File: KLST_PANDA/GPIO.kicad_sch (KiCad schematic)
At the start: 0 parts

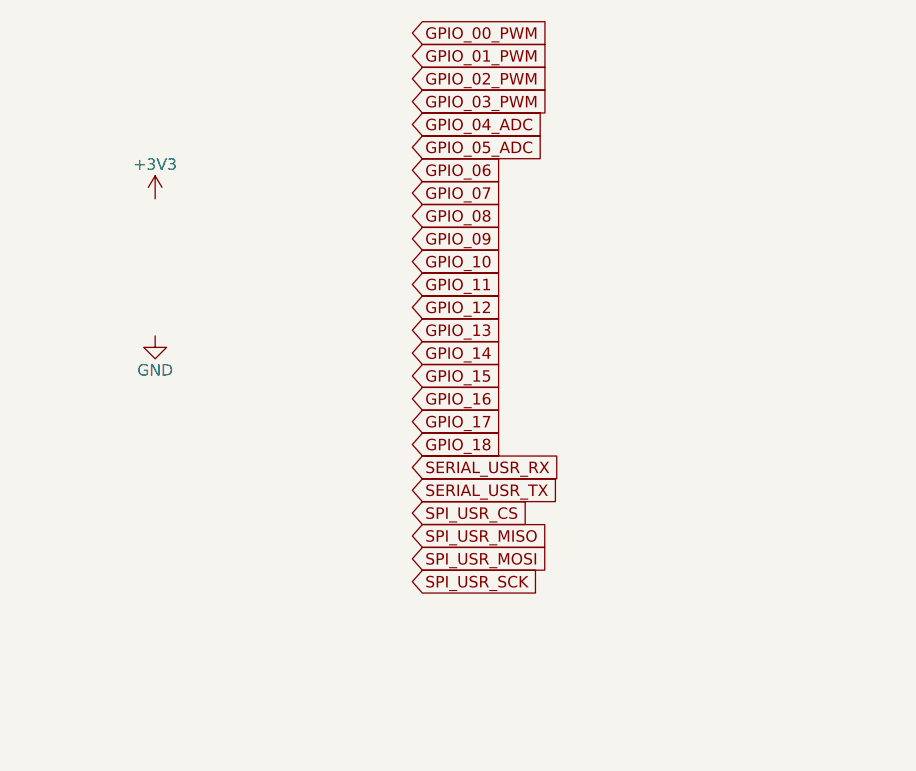
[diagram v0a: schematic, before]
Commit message: improved GPIO, updated schematics
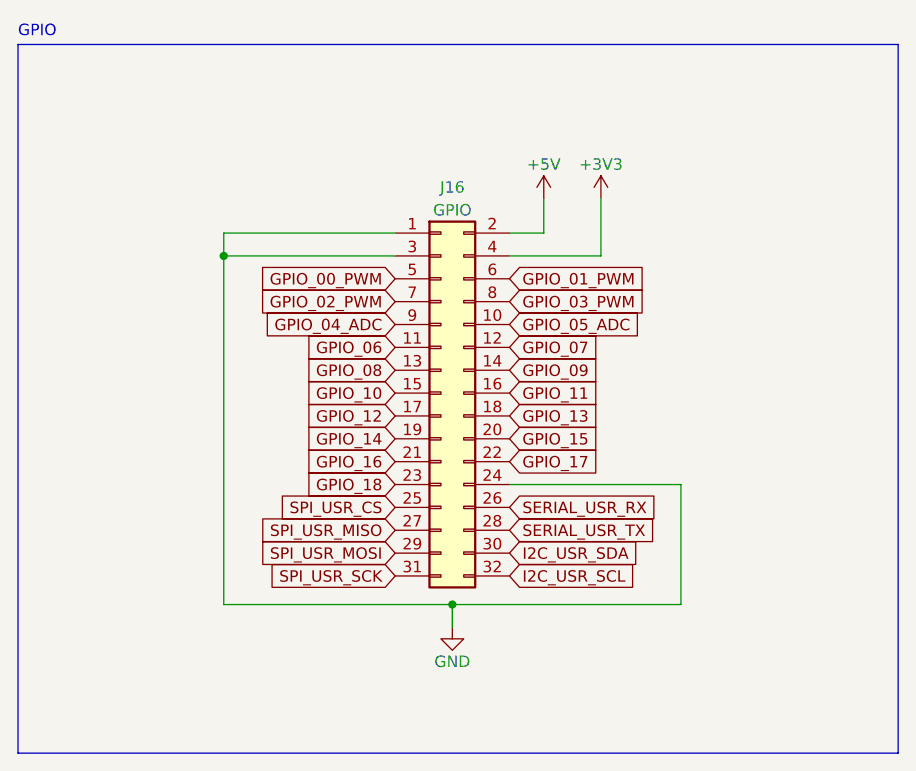
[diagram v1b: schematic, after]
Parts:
- added J16: GPIO, symbol Connector_Generic:Conn_02x16_Odd_Even
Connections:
- net +3V3: now also J16.4 (Pin_4)
- net GND: now also J16.1 (Pin_1), J16.24 (Pin_24), J16.3 (Pin_3)
- net GPIO_00_PWM: now also J16.5 (Pin_5)
- net GPIO_01_PWM: now also J16.6 (Pin_6)
- net GPIO_02_PWM: now also J16.7 (Pin_7)
- net GPIO_03_PWM: now also J16.8 (Pin_8)
- net GPIO_04_ADC: now also J16.9 (Pin_9)
- net GPIO_05_ADC: now also J16.10 (Pin_10)
- net GPIO_06: now also J16.11 (Pin_11)
- net GPIO_07: now also J16.12 (Pin_12)
- net GPIO_08: now also J16.13 (Pin_13)
- net GPIO_09: now also J16.14 (Pin_14)
- net GPIO_10: now also J16.15 (Pin_15)
- net GPIO_11: now also J16.16 (Pin_16)
- net GPIO_12: now also J16.17 (Pin_17)
- net GPIO_13: now also J16.18 (Pin_18)
- net GPIO_14: now also J16.19 (Pin_19)
- net GPIO_15: now also J16.20 (Pin_20)
- net GPIO_16: now also J16.21 (Pin_21)
- net GPIO_17: now also J16.22 (Pin_22)
- net GPIO_18: now also J16.23 (Pin_23)
- net SERIAL_USR_RX: now also J16.26 (Pin_26)
- net SERIAL_USR_TX: now also J16.28 (Pin_28)
- net SPI_USR_CS: now also J16.25 (Pin_25)
- net SPI_USR_MISO: now also J16.27 (Pin_27)
- net SPI_USR_MOSI: now also J16.29 (Pin_29)
- net SPI_USR_SCK: now also J16.31 (Pin_31)
- new net +5V: J16.2 (Pin_2)
- new net I2C_USR_SCL: J16.32 (Pin_32)
- new net I2C_USR_SDA: J16.30 (Pin_30)
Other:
- note added: "GPIO"

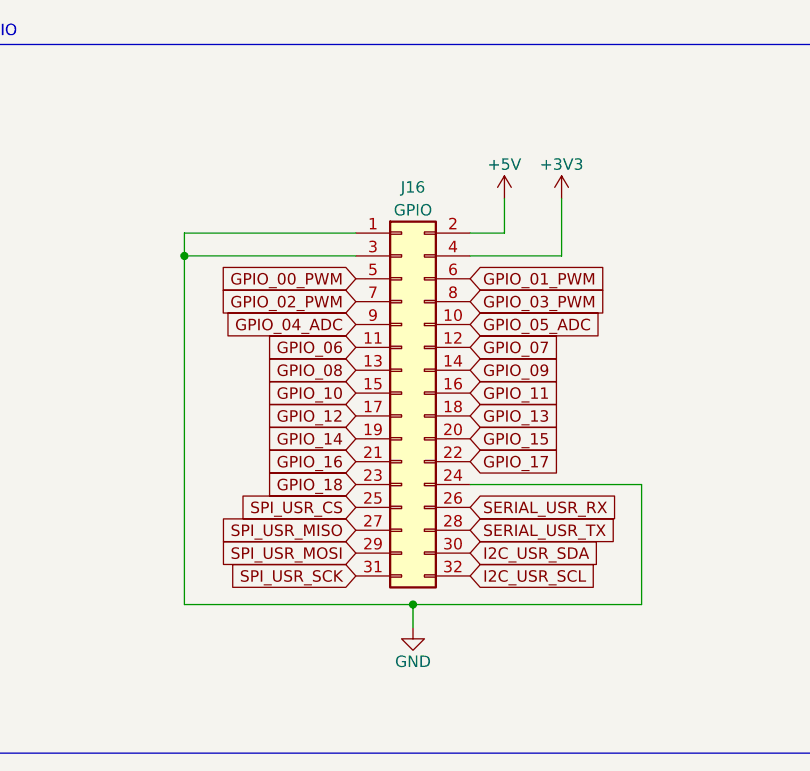
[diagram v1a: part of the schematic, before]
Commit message: added PDM interface ( and removed SAI )
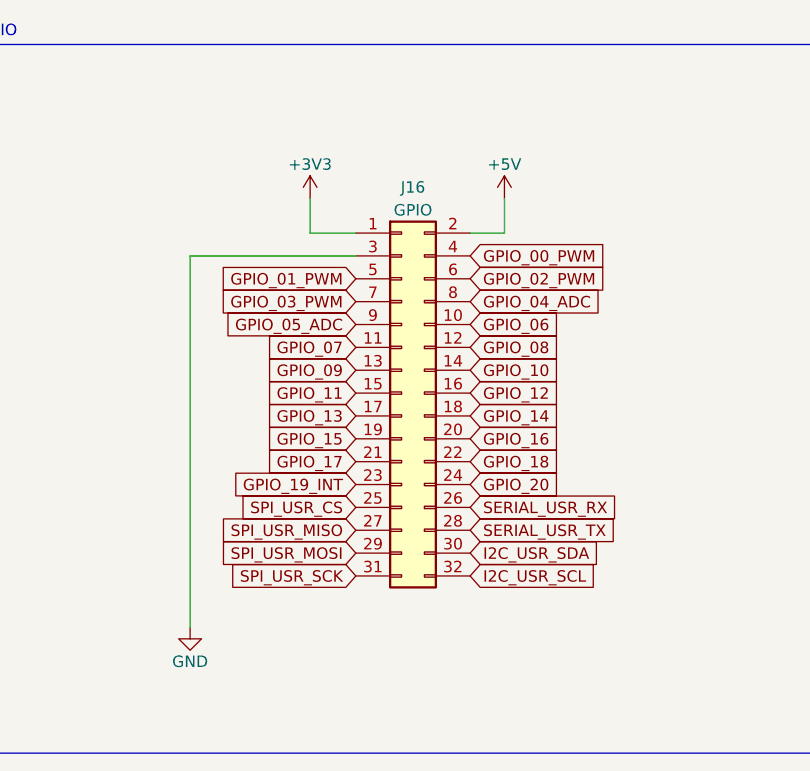
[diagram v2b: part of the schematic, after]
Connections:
- net +3V3: now also J16.1 (Pin_1); no longer J16.4 (Pin_4)
- net GND: no longer J16.1 (Pin_1), J16.24 (Pin_24)
- net GPIO_00_PWM: now also J16.4 (Pin_4); no longer J16.5 (Pin_5)
- net GPIO_01_PWM: now also J16.5 (Pin_5); no longer J16.6 (Pin_6)
- net GPIO_02_PWM: now also J16.6 (Pin_6); no longer J16.7 (Pin_7)
- net GPIO_03_PWM: now also J16.7 (Pin_7); no longer J16.8 (Pin_8)
- net GPIO_04_ADC: now also J16.8 (Pin_8); no longer J16.9 (Pin_9)
- net GPIO_05_ADC: now also J16.9 (Pin_9); no longer J16.10 (Pin_10)
- net GPIO_06: now also J16.10 (Pin_10); no longer J16.11 (Pin_11)
- net GPIO_07: now also J16.11 (Pin_11); no longer J16.12 (Pin_12)
- net GPIO_08: now also J16.12 (Pin_12); no longer J16.13 (Pin_13)
- net GPIO_09: now also J16.13 (Pin_13); no longer J16.14 (Pin_14)
- net GPIO_10: now also J16.14 (Pin_14); no longer J16.15 (Pin_15)
- net GPIO_11: now also J16.15 (Pin_15); no longer J16.16 (Pin_16)
- net GPIO_12: now also J16.16 (Pin_16); no longer J16.17 (Pin_17)
- net GPIO_13: now also J16.17 (Pin_17); no longer J16.18 (Pin_18)
- net GPIO_14: now also J16.18 (Pin_18); no longer J16.19 (Pin_19)
- net GPIO_15: now also J16.19 (Pin_19); no longer J16.20 (Pin_20)
- net GPIO_16: now also J16.20 (Pin_20); no longer J16.21 (Pin_21)
- net GPIO_17: now also J16.21 (Pin_21); no longer J16.22 (Pin_22)
- net GPIO_18: now also J16.22 (Pin_22); no longer J16.23 (Pin_23)
- new net GPIO_19_INT: J16.23 (Pin_23)
- new net GPIO_20: J16.24 (Pin_24)

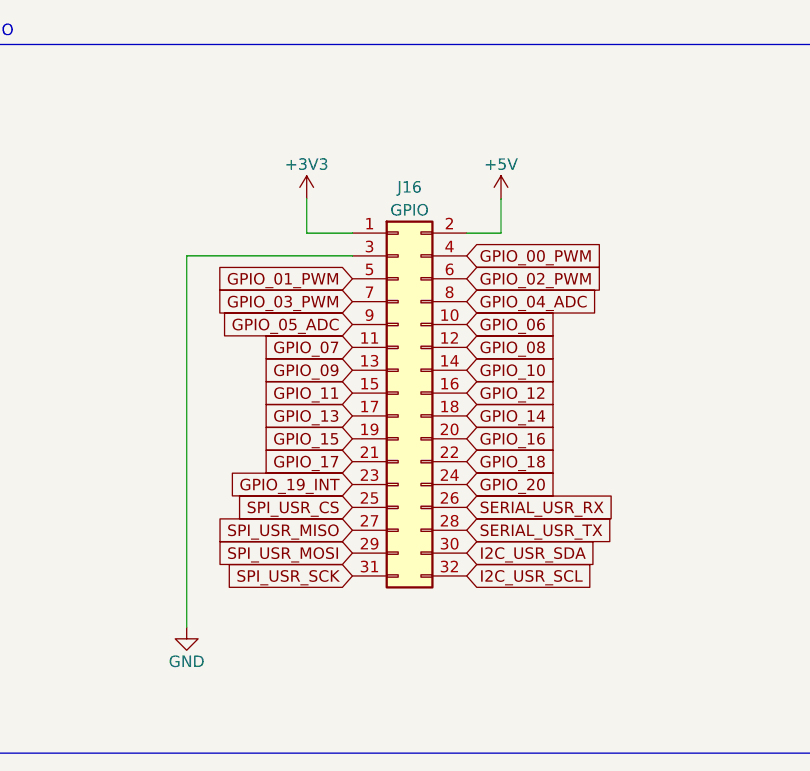
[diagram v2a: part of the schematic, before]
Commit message: added mechanical keys, updated audio jacks, minor changes
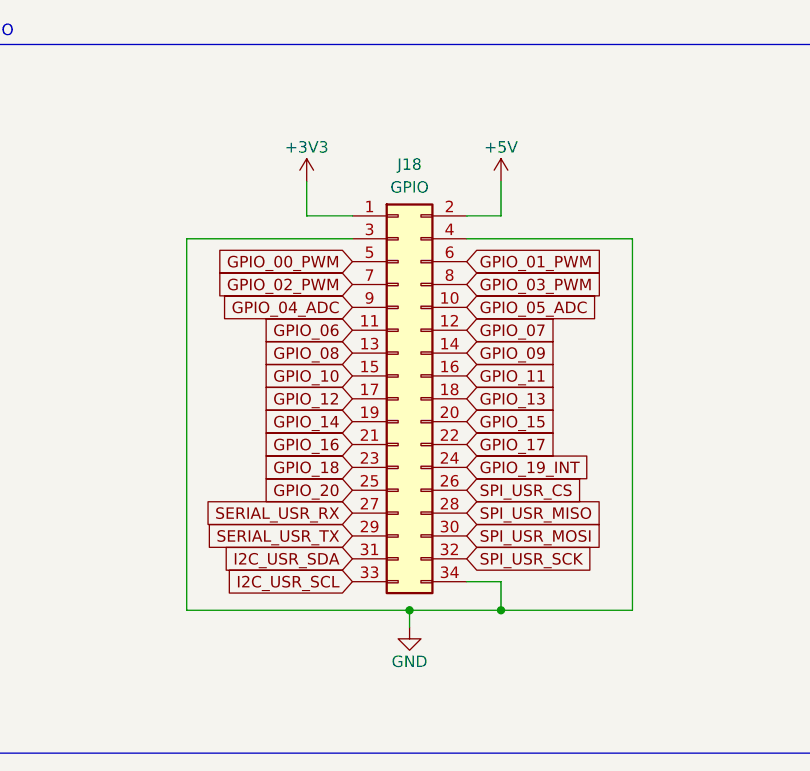
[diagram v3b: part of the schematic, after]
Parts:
- removed J16: GPIO, symbol Connector_Generic:Conn_02x16_Odd_Even
- added J18: GPIO, Connector_IDC:IDC-Header_2x17_P2.54mm_Horizontal, symbol Connector_Generic:Conn_02x17_Odd_Even
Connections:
- net +3V3: now also J18.1 (Pin_1)
- net +5V: now also J18.2 (Pin_2)
- net GND: now also J18.3 (Pin_3), J18.34 (Pin_34), J18.4 (Pin_4)
- net GPIO_00_PWM: now also J18.5 (Pin_5)
- net GPIO_01_PWM: now also J18.6 (Pin_6)
- net GPIO_02_PWM: now also J18.7 (Pin_7)
- net GPIO_03_PWM: now also J18.8 (Pin_8)
- net GPIO_04_ADC: now also J18.9 (Pin_9)
- net GPIO_05_ADC: now also J18.10 (Pin_10)
- net GPIO_06: now also J18.11 (Pin_11)
- net GPIO_07: now also J18.12 (Pin_12)
- net GPIO_08: now also J18.13 (Pin_13)
- net GPIO_09: now also J18.14 (Pin_14)
- net GPIO_10: now also J18.15 (Pin_15)
- net GPIO_11: now also J18.16 (Pin_16)
- net GPIO_12: now also J18.17 (Pin_17)
- net GPIO_13: now also J18.18 (Pin_18)
- net GPIO_14: now also J18.19 (Pin_19)
- net GPIO_15: now also J18.20 (Pin_20)
- net GPIO_16: now also J18.21 (Pin_21)
- net GPIO_17: now also J18.22 (Pin_22)
- net GPIO_18: now also J18.23 (Pin_23)
- net GPIO_19_INT: now also J18.24 (Pin_24)
- net GPIO_20: now also J18.25 (Pin_25)
- net I2C_USR_SCL: now also J18.33 (Pin_33)
- net I2C_USR_SDA: now also J18.31 (Pin_31)
- net SERIAL_USR_RX: now also J18.27 (Pin_27)
- net SERIAL_USR_TX: now also J18.29 (Pin_29)
- net SPI_USR_CS: now also J18.26 (Pin_26)
- net SPI_USR_MISO: now also J18.28 (Pin_28)
- net SPI_USR_MOSI: now also J18.30 (Pin_30)
- net SPI_USR_SCK: now also J18.32 (Pin_32)

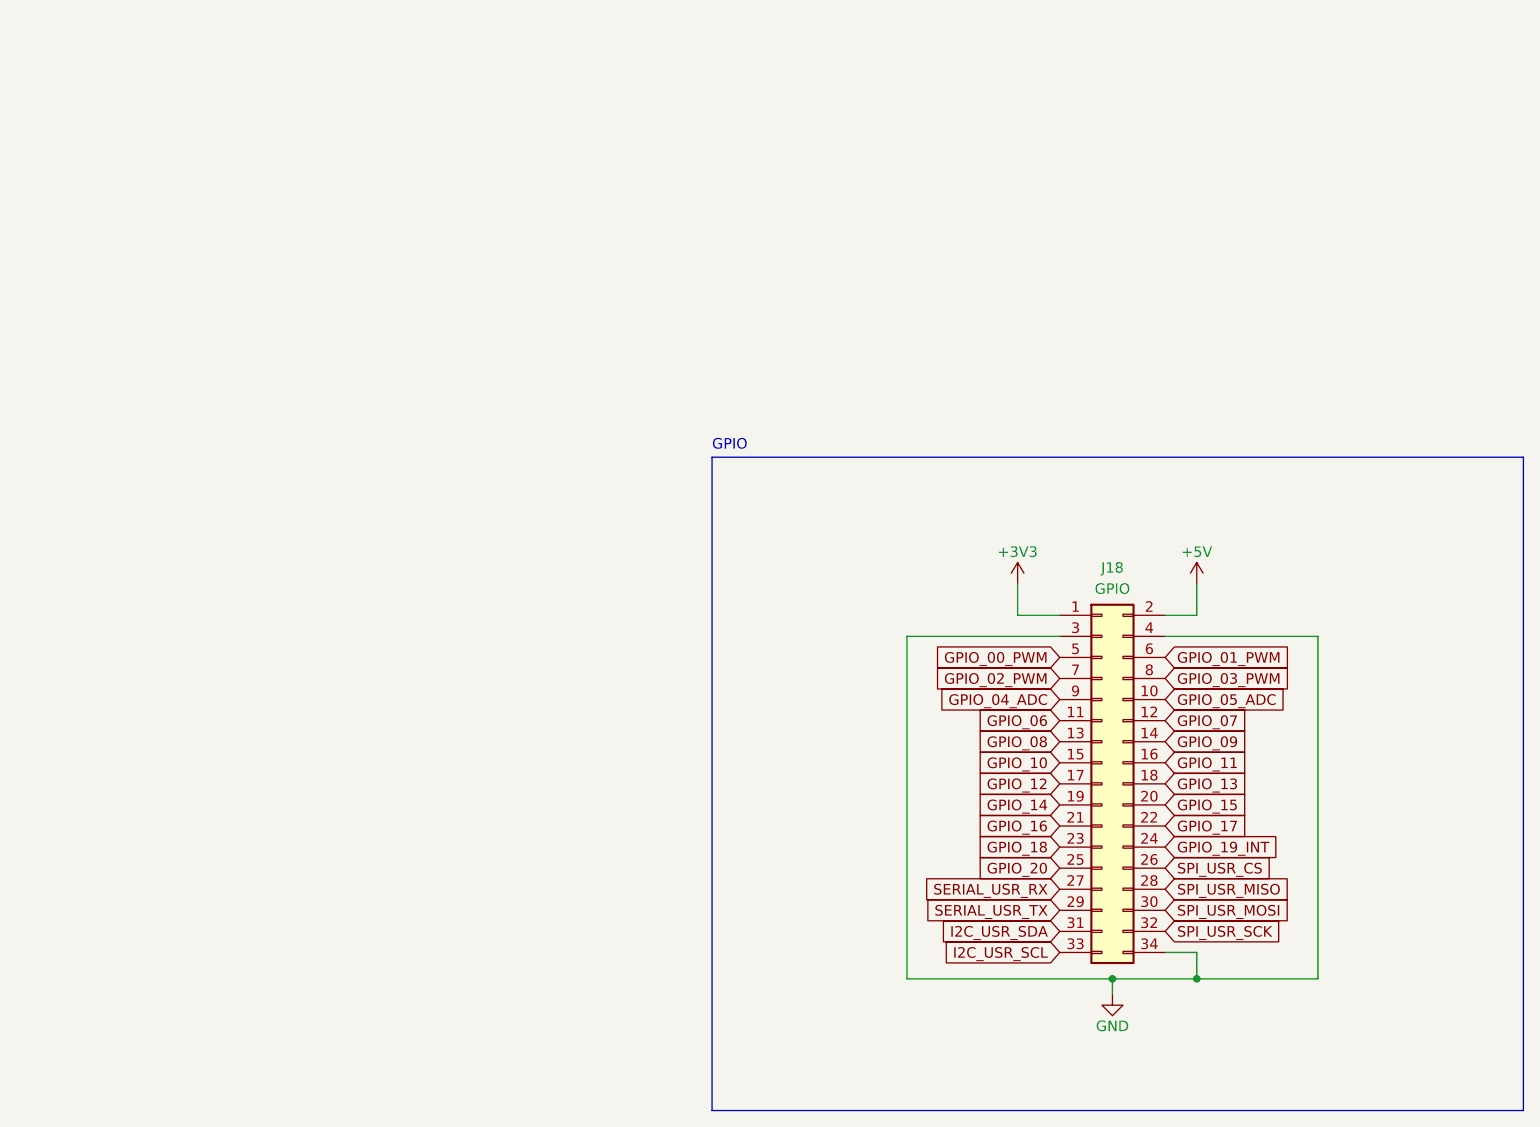
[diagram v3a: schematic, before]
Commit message: moved core (MCU) to sheet, cleaned up sheets
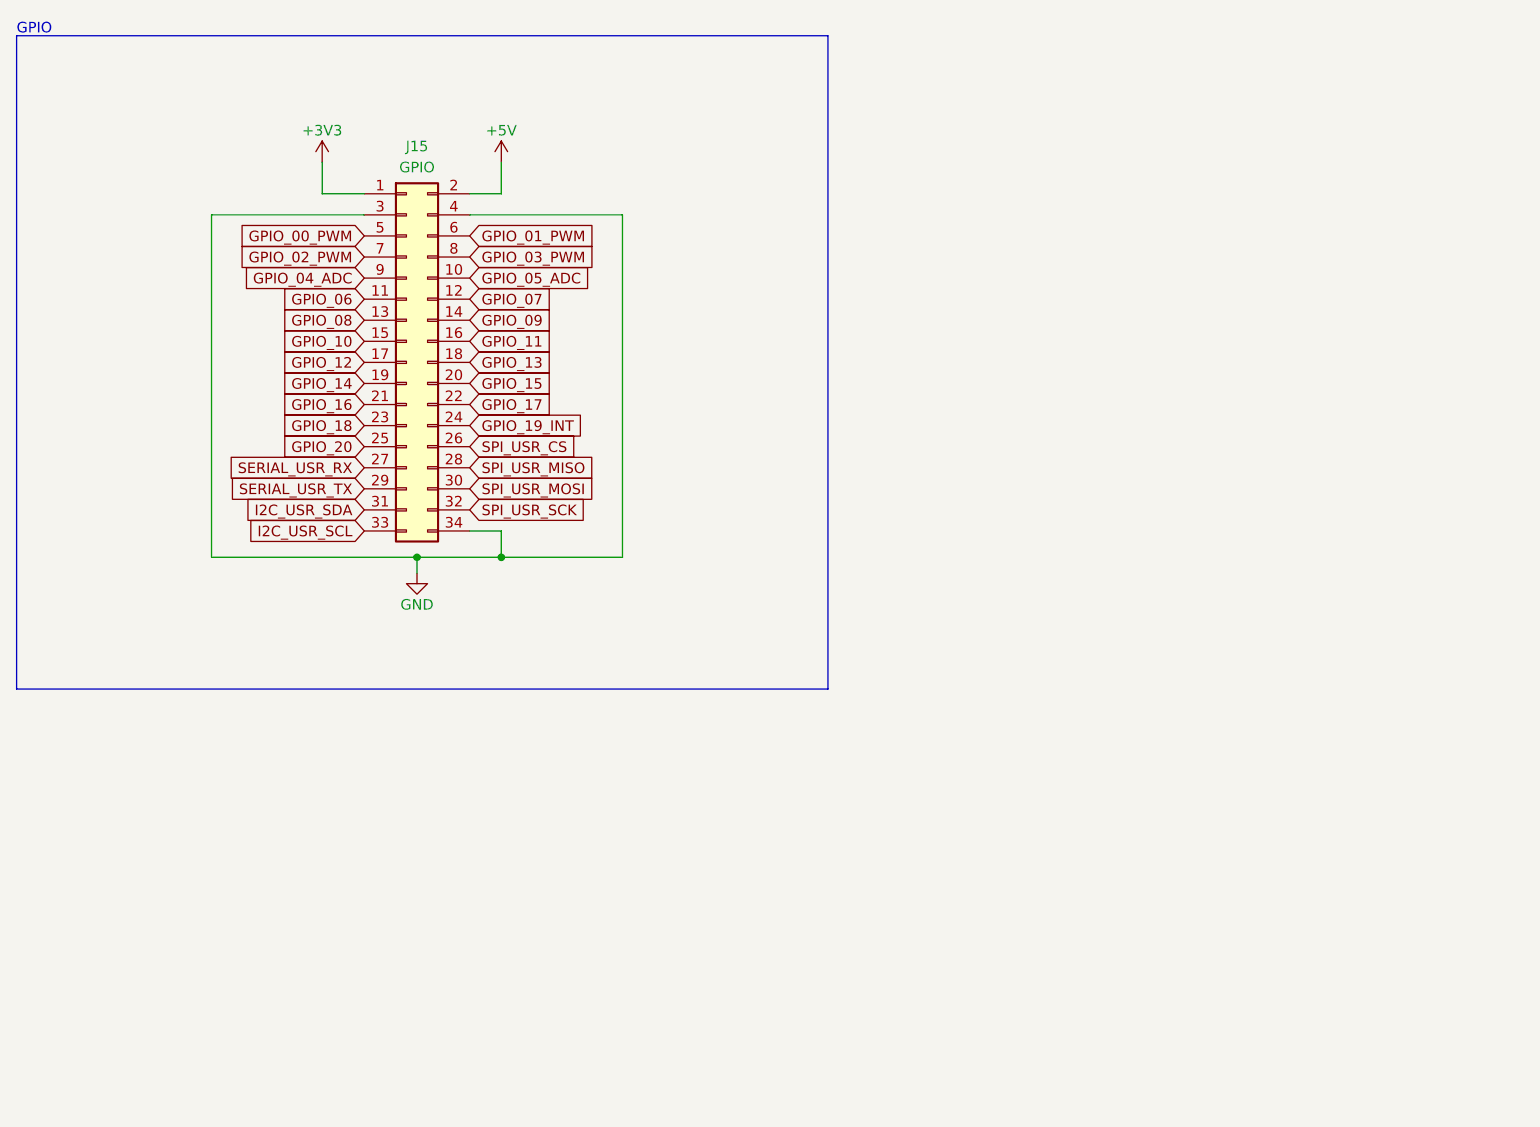
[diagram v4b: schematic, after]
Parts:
- renumbered J18 to J15
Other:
- moved on the sheet: J15

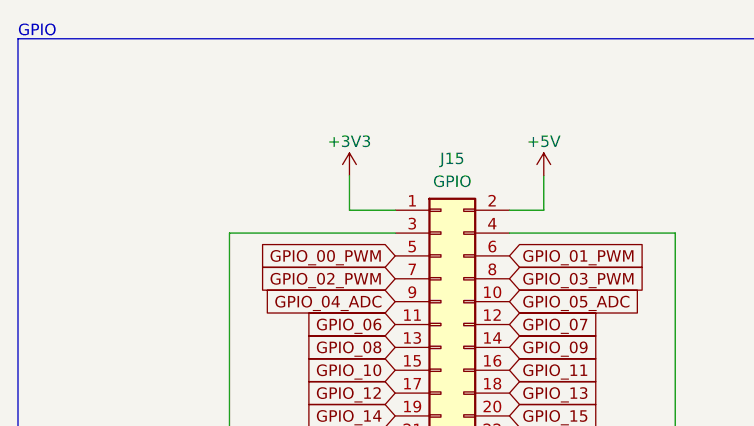
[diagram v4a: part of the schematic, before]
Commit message: started cleaning up schematic ( addressing DRC errors/warning ) (WIP)
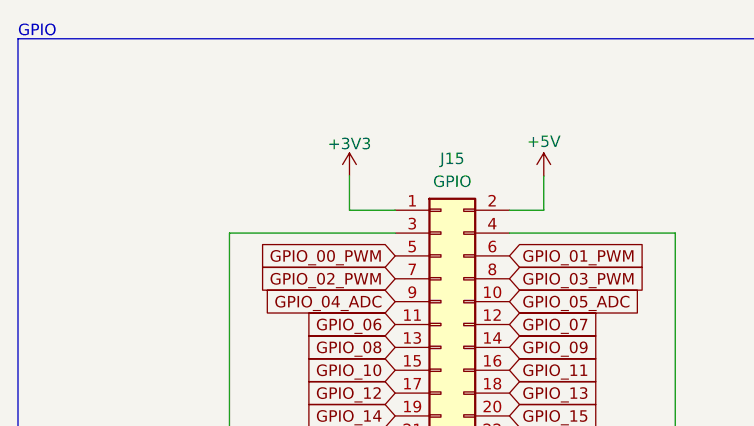
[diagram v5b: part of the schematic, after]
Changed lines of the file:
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@@
         )
         (path "/b4513875-4c57-4720-bcc5-43ead67fe18f/6bb3f144-c620-4528-bce8-cfaf92f97449"
-          (reference "#PWR086") (unit 1)
+          (reference "#PWR087") (unit 1)
         )
       )
@@
         )
         (path "/b4513875-4c57-4720-bcc5-43ead67fe18f/6bb3f144-c620-4528-bce8-cfaf92f97449"
-          (reference "#PWR087") (unit 1)
+          (reference "#PWR088") (unit 1)
         )
       )
@@
       (effects (font (size 1.27 1.27)) hide)
     )
-    (property "Value" "+3V3" (at 52.07 26.67 0)
+    (property "Value" "+3V3" (at 52.07 26.924 0)
       (effects (font (size 1.27 1.27)))
     )
@@
         )
         (path "/b4513875-4c57-4720-bcc5-43ead67fe18f/6bb3f144-c620-4528-bce8-cfaf92f97449"
-          (reference "#PWR085") (unit 1)
+          (reference "#PWR086") (unit 1)
         )
       )
